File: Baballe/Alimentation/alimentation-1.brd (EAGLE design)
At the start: 30 x 30 mm, 17 parts, among them Q1 2.5A/30V, U1 MCP73831, U2 3.3V

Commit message: V2 de la Baballe
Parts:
- moved LED1 14.3 mm to (8.51, 55.5)
- moved C3 12.6 mm to (20.7, 67.1), turned to 90 degrees
- moved R5 12.5 mm to (8.85, 67.0), turned to 90 degrees
- moved R6 9.61 mm to (6.69, 67.0), turned to 270 degrees
- moved C1 9.39 mm to (19.1, 57.0), turned to 270 degrees
- moved R1 8.84 mm to (12.7, 66.1), turned to 90 degrees
- moved SUPPLY 8.58 mm to (27.9, 56.5), turned to 90 degrees
- moved D1 6.82 mm to (16.2, 69.4), turned to 180 degrees
- moved R2 6.00 mm to (7.91, 59.1), turned to 0 degrees
- moved U1 3.00 mm to (13.8, 61.3)
- moved C2 2.52 mm to (23.0, 61.2), turned to 270 degrees
- moved BAT 2.28 mm to (25.5, 79.6), turned to 0 degrees
- moved I/O 2.28 mm to (4.06, 56.1)
- moved USB 2.00 mm to (4.27, 79.7)
- moved R3 1.99 mm to (7.90, 62.1), turned to 180 degrees
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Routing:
- net VIN: track 23.1 -> 44.3 mm, vias 0 -> 1
- net V_BATT: track 46.1 -> 33.5 mm
- net VUSB: track 43.4 -> 55.4 mm, vias 3 -> 2
- net VCC_2: track 27.4 -> 16.9 mm
- net N$2: track 3.80 -> 12.5 mm
- net V_BAT_MESURE: track 11.6 -> 5.44 mm
- net N$4: track 9.75 -> 4.80 mm
- net N$1: track 7.58 -> 3.73 mm
- net VCC: track 9.08 -> 11.8 mm
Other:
- board size 30 x 30 mm -> 37.9 x 37.9 mm

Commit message: Baballe en attente de vérification finale
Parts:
- moved SUPPLY 0.56 mm to (28.0, 56.0)
- moved I/O 0.11 mm to (4.01, 56.0)
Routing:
- net VIN: track 44.3 -> 58.9 mm, vias 1 -> 2
- net V_BATT: track 33.5 -> 34.9 mm
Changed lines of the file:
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@@
 <plain>
 <circle x="16" y="68" radius="18.94386875" width="0.1" layer="20"/>
-<circle x="16" y="68" radius="20.09975" width="0.1" layer="47"/>
 <hole x="16" y="80" drill="15"/>
 </plain>
@@
 </element>
 <element name="USB" library="SparkFun-Connectors" package="1X02_NO_SILK" value="USB" x="4.266759375" y="79.7352"/>
-<element name="I/O" library="SparkFun-Connectors" package="1X06_NO_SILK" value="I/O" x="4.055925" y="56.08016875" rot="R90">
-<attribute name="PROD_ID" value="CONN-08437" x="4.055925" y="56.08016875" size="1.778" layer="27" rot="R90" display="off"/>
-</element>
-<element name="SUPPLY" library="SparkFun-Connectors" package="1X05_NO_SILK" value="SUPPLY" x="27.878128125" y="56.5292125" rot="R90"/>
+<element name="I/O" library="SparkFun-Connectors" package="1X06_NO_SILK" value="I/O" x="4.005925" y="55.98016875" rot="R90">
+<attribute name="PROD_ID" value="CONN-08437" x="4.005925" y="55.98016875" size="1.778" layer="27" rot="R90" display="off"/>
+</element>
+<element name="SUPPLY" library="SparkFun-Connectors" package="1X05_NO_SILK" value="SUPPLY" x="27.978128125" y="55.9792125" rot="R90"/>
 </elements>
 <signals>
@@
 <wire x1="27.5" y1="66.5" x2="21" y2="66.5" width="0.5" layer="1"/>
 <wire x1="21" y1="66.5" x2="20.74939375" y2="66.19145" width="0.5" layer="1"/>
-<wire x1="27.5" y1="66.5" x2="27.878128125" y2="66.6892125" width="0.5" layer="1"/>
+<wire x1="27.5" y1="66.5" x2="27.978128125" y2="66.1392125" width="0.5" layer="1"/>
 </signal>
 <signal name="VIN" class="1">
@@
 <contactref element="U2" pad="3"/>
 <contactref element="SUPPLY" pad="3"/>
-<wire x1="22.96" y1="62.14" x2="23" y2="62.14" width="0.254" layer="1"/>
 <wire x1="23" y1="62.14" x2="23" y2="62" width="0.254" layer="1"/>
-<wire x1="27.5" y1="69.5" x2="17.5" y2="69.5" width="0.5" layer="1"/>
+<wire x1="27.5" y1="69.5" x2="18" y2="69.5" width="0.5" layer="1"/>
+<wire x1="18" y1="69.5" x2="17.5" y2="69.5" width="0.5" layer="1"/>
 <wire x1="30" y1="67" x2="27.5" y2="69.5" width="0.5" layer="1"/>
 <wire x1="30" y1="62" x2="30" y2="67" width="0.5" layer="1"/>
-<wire x1="28" y1="62" x2="30" y2="62" width="0.5" layer="1"/>
 <wire x1="17.5" y1="69.5" x2="17.395" y2="69.4" width="0.5" layer="1"/>
-<wire x1="28" y1="62" x2="27.878128125" y2="61.6092125" width="0.5" layer="1"/>
 <wire x1="16.5" y1="55" x2="16" y2="55.5" width="0.5" layer="1"/>
 <wire x1="17.5" y1="55" x2="16.5" y2="55" width="0.5" layer="1"/>
 <wire x1="26" y1="55" x2="17.5" y2="55" width="0.5" layer="16"/>
 <wire x1="26" y1="60" x2="26" y2="55" width="0.5" layer="16"/>
-<wire x1="27.5" y1="61.5" x2="26" y2="60" width="0.5" layer="16"/>
 <wire x1="16" y1="55.5" x2="15.84" y2="55.45" width="0.5" layer="1"/>
-<wire x1="27.5" y1="61.5" x2="27.878128125" y2="61.6092125" width="0.5" layer="16"/>
-<wire x1="27.5" y1="62" x2="23" y2="62" width="0.5" layer="1"/>
 <wire x1="23" y1="62" x2="22.96" y2="62.14" width="0.5" layer="1"/>
-<wire x1="27.5" y1="62" x2="27.878128125" y2="61.6092125" width="0.5" layer="1"/>
 <via x="17.5" y="55" extent="1-16" drill="0.6096"/>
-<wire x1="22.96" y1="62.14" x2="17.8599" y2="62.18" width="0" layer="19" extent="1-1"/>
-<wire x1="17.8599" y1="60.28" x2="17.8599" y2="62.18" width="0" layer="19" extent="1-1"/>
+<wire x1="22.96" y1="62.14" x2="23" y2="62.14" width="0.5" layer="1"/>
+<wire x1="17.8599" y1="62.18" x2="18" y2="62.18" width="0.5" layer="1"/>
+<wire x1="18" y1="62.18" x2="18" y2="69.5" width="0.5" layer="1"/>
+<wire x1="17.8599" y1="60.28" x2="17" y2="60.28" width="0.5" layer="1"/>
+<wire x1="17" y1="60.28" x2="17" y2="59" width="0.5" layer="1"/>
+<via x="17" y="59" extent="1-16" drill="0.6"/>
+<wire x1="17.5" y1="55" x2="17" y2="55" width="0.5" layer="16"/>
+<wire x1="17" y1="55" x2="17" y2="59" width="0.5" layer="16"/>
+<wire x1="23" y1="62" x2="25" y2="62" width="0.5" layer="1"/>
+<wire x1="25" y1="62" x2="26" y2="61" width="0.5" layer="1"/>
+<wire x1="26" y1="61" x2="28.037340625" y2="61" width="0.5" layer="1"/>
+<wire x1="29" y1="61" x2="30" y2="62" width="0.5" layer="1"/>
+<wire x1="26" y1="60" x2="27" y2="61" width="0.5" layer="16"/>
+<wire x1="27" y1="61" x2="27.918915625" y2="61" width="0.5" layer="16"/>
+<wire x1="27.918915625" y1="61" x2="27.978128125" y2="61.0592125" width="0.5" layer="16"/>
+<wire x1="27.978128125" y1="61.0592125" x2="27.978128125" y2="61.021871875" width="0.5" layer="16"/>
+<wire x1="27.978128125" y1="61.021871875" x2="28" y2="61" width="0.5" layer="16"/>
+<wire x1="29" y1="61" x2="28.037340625" y2="61" width="0.5" layer="1"/>
+<wire x1="28.037340625" y1="61" x2="27.978128125" y2="61.0592125" width="0.5" layer="1"/>
 </signal>
 <signal name="V_BATT" class="1">
@@
 <contactref element="SUPPLY" pad="4"/>
 <wire x1="11" y1="68" x2="9" y2="68" width="0.5" layer="1"/>
-<wire x1="26" y1="68" x2="25.5" y2="68" width="0.5" layer="16"/>
-<wire x1="25.5" y1="68" x2="11" y2="68" width="0.5" layer="16"/>
-<wire x1="26" y1="66" x2="26" y2="68" width="0.5" layer="16"/>
-<wire x1="27.5" y1="64.5" x2="26" y2="66" width="0.5" layer="16"/>
+<wire x1="25.5" y1="68" x2="25" y2="68" width="0.5" layer="16"/>
+<wire x1="25" y1="68" x2="11" y2="68" width="0.5" layer="16"/>
+<wire x1="25" y1="65" x2="25" y2="68" width="0.5" layer="16"/>
+<wire x1="26.5" y1="63.5" x2="25" y2="65" width="0.5" layer="16"/>
 <wire x1="9" y1="68" x2="8.845" y2="67.91725625" width="0.5" layer="1"/>
-<wire x1="27.5" y1="64.5" x2="27.878128125" y2="64.1492125" width="0.5" layer="16"/>
+<wire x1="26.5" y1="63.5" x2="27.978128125" y2="63.5992125" width="0.5" layer="16"/>
 <wire x1="25.5" y1="68" x2="25.5" y2="79.5" width="0.5" layer="16"/>
 <wire x1="25.5" y1="79.5" x2="25.53" y2="79.645" width="0.5" layer="16"/>
@@
 <wire x1="4.5" y1="66.5" x2="6.5" y2="66.5" width="0.127" layer="1"/>
 <wire x1="6.5" y1="66.5" x2="6.69" y2="66.1240625" width="0.127" layer="1"/>
-<wire x1="4.5" y1="66.5" x2="4.055925" y2="66.24016875" width="0.127" layer="1"/>
+<wire x1="4.5" y1="66.5" x2="4.005925" y2="66.14016875" width="0.127" layer="1"/>
 </signal>
 <signal name="VCC_2">
@@
 <wire x1="27.5" y1="59" x2="20.5" y2="59" width="0.127" layer="1"/>
 <wire x1="19.5" y1="58" x2="19.07986875" y2="57.86878125" width="0.127" layer="1"/>
-<wire x1="27.5" y1="59" x2="27.878128125" y2="59.0692125" width="0.127" layer="1"/>
+<wire x1="27.5" y1="59" x2="27.978128125" y2="58.5192125" width="0.127" layer="1"/>
 </signal>
 </signals>

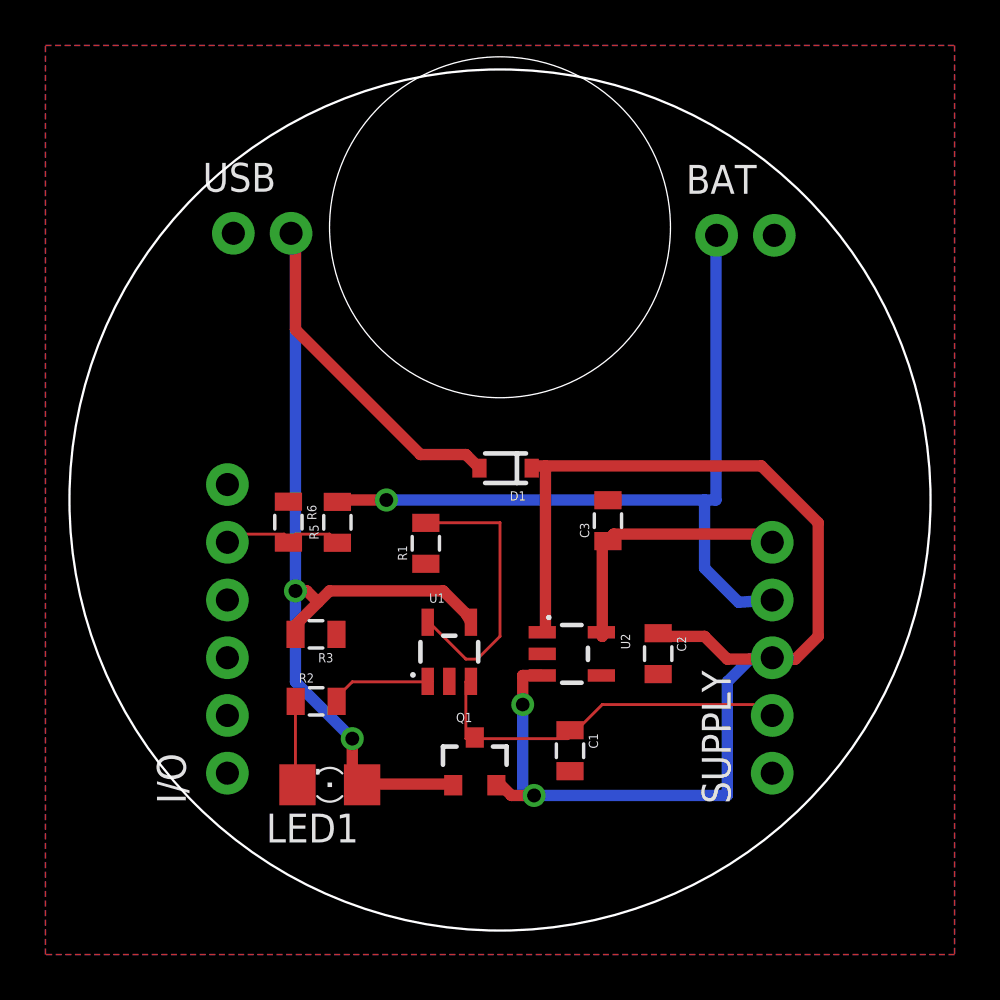
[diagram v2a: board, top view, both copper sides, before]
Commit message: Correction des cartes alim et boutons suite à une erreur détectée lors de l'impression
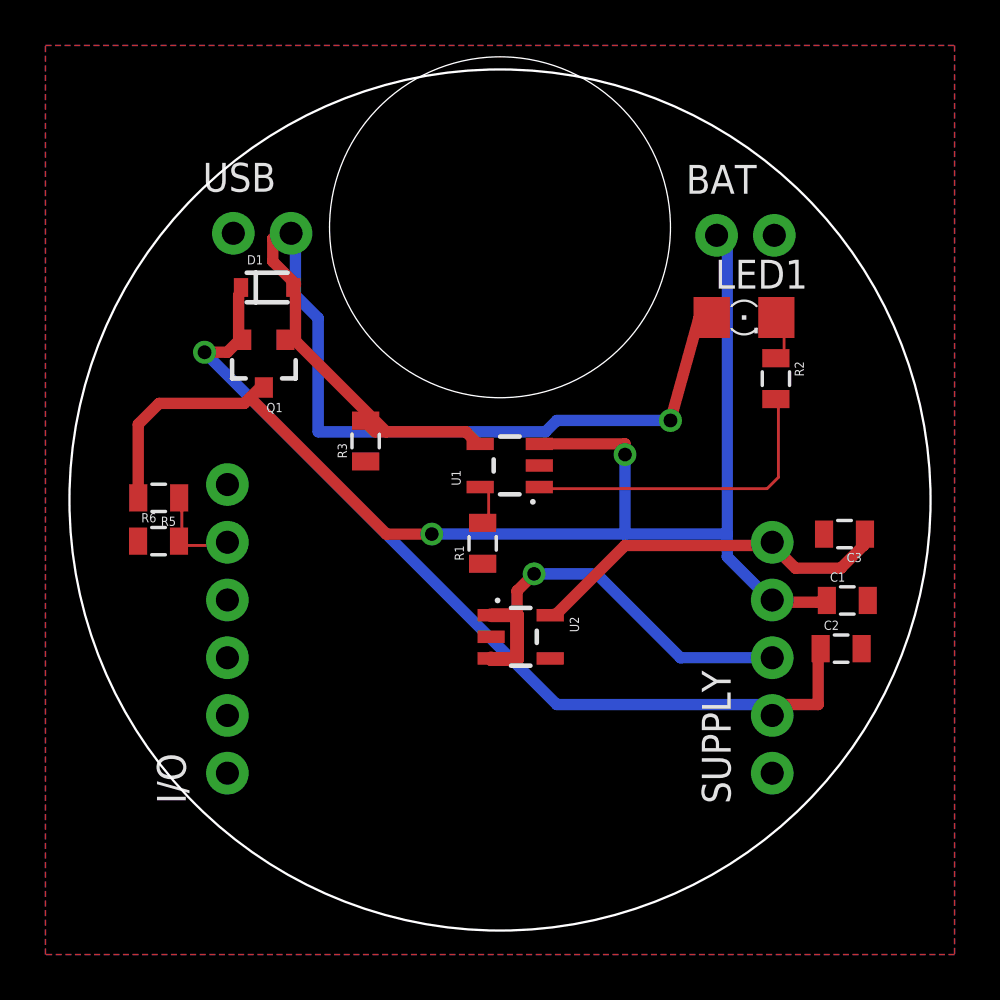
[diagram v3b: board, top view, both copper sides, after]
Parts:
- moved LED1 27.5 mm to (26.7, 76.0), turned to 0 degrees
- moved R2 24.7 mm to (28.1, 73.3), turned to 270 degrees
- moved Q1 19.9 mm to (5.61, 74.0), turned to 180 degrees
- moved C1 13.9 mm to (31.3, 63.6), turned to 0 degrees
- moved D1 13.2 mm to (5.75, 77.3), turned to 0 degrees
- moved C3 10.4 mm to (31.2, 66.5), turned to 180 degrees
- moved R3 8.78 mm to (10.1, 70.6), turned to 90 degrees
- moved U1 8.62 mm to (16.4, 69.5), turned to 90 degrees
- moved C2 8.05 mm to (31.0, 61.5), turned to 0 degrees
- moved R5 7.94 mm to (0.98, 68.1), turned to 180 degrees
- moved R6 5.77 mm to (0.98, 66.2), turned to 0 degrees
- moved R1 2.50 mm to (15.2, 66.1)
- moved U2 2.37 mm to (16.9, 62.0)
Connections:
- net VCC_2: now also SUPPLY.3, U2.1, U2.3; no longer C1.1, Q1.3, SUPPLY.2, U1.3
- net VIN: now also SUPPLY.2; no longer SUPPLY.3, U2.1, U2.3
- net V_BATT: now also C1.1, Q1.3, U1.3
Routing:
- net V_BATT: track 34.9 -> 60.9 mm, vias 1 -> 2
- net VIN: track 58.9 -> 40.8 mm, vias 2 -> 1
- net N$2: track 12.5 -> 2.14 mm
- net N$4: track 4.80 -> 14.4 mm
- net VUSB: track 55.4 -> 47.9 mm, vias 2 -> 1
- net VCC: track 12.0 -> 16.5 mm
- net N$1: track 3.73 -> 2.28 mm
- net VCC_2: track 17.1 -> 18.4 mm, vias 0 -> 1
- net V_BAT_MESURE: track 5.53 -> 4.31 mm
- net GND: track 0.00 -> 0.59 mm
